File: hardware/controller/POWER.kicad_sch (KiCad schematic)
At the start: 21 parts, among them IC201 TPS63000IDRCRQ1, J201 1769

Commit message: a
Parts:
- added NT201: NetTie, NetTie:NetTie-2_SMD_Pad0.5mm, symbol SamacSys_Parts:NetTie
- D201: footprint SMF50A_R1_00001 -> SamacSys_Parts:SMF50A_R1_00001
- IC201: footprint SamacSys_Parts:TPS63000IDRCRQ1 -> TPS63000IDRCRQ1
- R201: footprint RESC1608X55N -> SamacSys_Parts:RESC1608X55N
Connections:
- net GND: now also NT201.1
- net GNDPWR: now also NT201.2
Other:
- note removed: "Connect control ground to common ground near GND pin"
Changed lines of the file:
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@@
 		)
 	)
-	(text "Connect control ground to \ncommon ground near GND pin"
-		(exclude_from_sim no)
-		(at 247.396 148.336 0)
-		(effects
-			(font
-				(size 1.27 1.27)
-			)
-		)
-	)
 	(text "Hierarchical Pins"
 		(exclude_from_sim no)
@@
 	)
 	(junction
+		(at 219.71 146.05)
+		(diameter 0)
+		(color 0 0 0 0)
+	)
+	(junction
 		(at 133.35 110.49)
 		(diameter 0)
@@
 	)
 	(junction
+		(at 209.55 146.05)
+		(diameter 0)
+		(color 0 0 0 0)
+	)
+	(junction
+		(at 204.47 146.05)
+		(diameter 0)
+		(color 0 0 0 0)
+	)
+	(junction
 		(at 246.38 114.3)
 		(diameter 0)
@@
 	)
 	(junction
-		(at 209.55 146.05)
-		(diameter 0)
-		(color 0 0 0 0)
-	)
-	(junction
 		(at 250.19 124.46)
 		(diameter 0)
@@
 	(wire
 		(pts
-			(xy 207.01 146.05) (xy 207.01 142.24)
-		)
-		(stroke
-			(width 0)
-			(type default)
-		)
-	)
-	(wire
-		(pts
 			(xy 186.69 110.49) (xy 195.58 110.49)
 		)
@@
 	(wire
 		(pts
-			(xy 204.47 142.24) (xy 204.47 149.86)
+			(xy 204.47 142.24) (xy 204.47 146.05)
 		)
 		(stroke
@@
 	(wire
 		(pts
-			(xy 207.01 146.05) (xy 209.55 146.05)
+			(xy 88.9 110.49) (xy 91.44 110.49)
 		)
 		(stroke
@@
 	(wire
 		(pts
-			(xy 88.9 110.49) (xy 91.44 110.49)
+			(xy 186.69 119.38) (xy 186.69 121.92)
 		)
 		(stroke
@@
 	(wire
 		(pts
-			(xy 186.69 119.38) (xy 186.69 121.92)
+			(xy 208.28 146.05) (xy 209.55 146.05)
 		)
 		(stroke
@@
 	(wire
 		(pts
+			(xy 222.25 146.05) (xy 219.71 146.05)
+		)
+		(stroke
+			(width 0)
+			(type default)
+		)
+	)
+	(wire
+		(pts
 			(xy 133.35 110.49) (xy 139.7 110.49)
 		)
@@
 	(wire
 		(pts
+			(xy 222.25 142.24) (xy 222.25 146.05)
+		)
+		(stroke
+			(width 0)
+			(type default)
+		)
+	)
+	(wire
+		(pts
 			(xy 173.99 114.3) (xy 173.99 110.49)
 		)
@@
 	(wire
 		(pts
+			(xy 204.47 146.05) (xy 204.47 149.86)
+		)
+		(stroke
+			(width 0)
+			(type default)
+		)
+	)
+	(wire
+		(pts
 			(xy 33.02 71.12) (xy 76.2 71.12)
 		)
@@
 	)
 	(symbol
-		(lib_id "power:GNDPWR")
-		(at 252.73 151.13 0)
-		(unit 1)
-		(exclude_from_sim no)
-		(in_bom yes)
-		(on_board yes)
-		(dnp no)
-		(fields_autoplaced yes)
-		(property "Reference" "#PWR0217"
-			(at 252.73 156.21 0)
-			(effects
-				(font
-					(size 1.27 1.27)
-				)
-				(hide yes)
-			)
-		)
-		(property "Value" "GNDPWR"
-			(at 252.603 154.94 0)
-			(effects
-				(font
-					(size 1.27 1.27)
-				)
-			)
-		)
-		(property "Footprint" ""
-			(at 252.73 152.4 0)
-			(effects
-				(font
-					(size 1.27 1.27)
-				)
-				(hide yes)
-			)
-		)
-		(property "Datasheet" ""
-			(at 252.73 152.4 0)
-			(effects
-				(font
-					(size 1.27 1.27)
-				)
-				(hide yes)
-			)
-		)
-		(property "Description" "Power symbol creates a global label with name \"GNDPWR\" , global ground"
-			(at 252.73 151.13 0)
-			(effects
-				(font
-					(size 1.27 1.27)
-				)
-				(hide yes)
-			)
-		)
-		(pin "1"
-		)
-		(instances
-			(project "controller"
-				(path "/869bea87-c885-4ead-826b-3f34ceacafad/e70789ad-230b-4d46-b635-87f45083e468"
-					(reference "#PWR0217")
-					(unit 1)
-				)
-			)
-		)
-	)
-	(symbol
 		(lib_id "Device:R")
 		(at 186.69 114.3 0)
@@
 			)
 		)
-		(property "Footprint" "RESC1608X55N"
+		(property "Footprint" "SamacSys_Parts:RESC1608X55N"
 			(at 200.66 210.49 0)
 			(effects
@@
 			)
 		)
-		(property "Footprint" "SMF50A_R1_00001"
+		(property "Footprint" "SamacSys_Parts:SMF50A_R1_00001"
 			(at -42.85 124.46 0)
 			(effects
@@
 	(symbol
 		(lib_id "power:GND")
-		(at 241.3 151.13 0)
-		(unit 1)
-		(exclude_from_sim no)
-		(in_bom yes)
-		(on_board yes)
-		(dnp no)
-		(fields_autoplaced yes)
-		(property "Reference" "#PWR0215"
-			(at 241.3 157.48 0)
-			(effects
-				(font
-					(size 1.27 1.27)
-				)
-				(hide yes)
-			)
-		)
-		(property "Value" "GND"
-			(at 241.3 156.21 0)
-			(effects
-				(font
-					(size 1.27 1.27)
-				)
-			)
-		)
-		(property "Footprint" ""
-			(at 241.3 151.13 0)
-			(effects
-				(font
-					(size 1.27 1.27)
-				)
-				(hide yes)
-			)
-		)
-		(property "Datasheet" ""
-			(at 241.3 151.13 0)
-			(effects
-				(font
-					(size 1.27 1.27)
-				)
-				(hide yes)
-			)
-		)
-		(property "Description" "Power symbol creates a global label with name \"GND\" , ground"
-			(at 241.3 151.13 0)
-			(effects
-				(font
-					(size 1.27 1.27)
-				)
-				(hide yes)
-			)
-		)
-		(pin "1"
-		)
-		(instances
-			(project "controller"
-				(path "/869bea87-c885-4ead-826b-3f34ceacafad/e70789ad-230b-4d46-b635-87f45083e468"
-					(reference "#PWR0215")
-					(unit 1)
-				)
-			)
-		)
-	)
-	(symbol
-		(lib_id "power:GND")
 		(at 139.7 134.62 0)
 		(unit 1)
@@
 	)
 	(symbol
+		(lib_id "SamacSys_Parts:NetTie")
+		(at 207.01 146.05 0)
+		(unit 1)
+		(exclude_from_sim no)
+		(in_bom no)
+		(on_board yes)
+		(dnp no)
+		(property "Reference" "NT201"
+			(at 197.358 142.24 0)
+			(effects
+				(font
+					(size 1.27 1.27)
+				)
+			)
+		)
+		(property "Value" "NetTie"
+			(at 197.358 144.78 0)
+			(effects
+				(font
+					(size 1.27 1.27)
+				)
+			)
+		)
+		(property "Footprint" "NetTie:NetTie-2_SMD_Pad0.5mm"
+			(at 207.01 146.05 0)
+			(effects
+				(font
+					(size 1.27 1.27)
+				)
+				(hide yes)
+			)
+		)
+		(property "Datasheet" "~"
+			(at 207.01 146.05 0)
+			(effects
+				(font
+					(size 1.27 1.27)
+				)
+				(hide yes)
+			)
+		)
+		(property "Description" "Net tie, 2 pins"
+			(at 207.01 146.05 0)
+			(effects
+				(font
+					(size 1.27 1.27)
+				)
+				(hide yes)
+			)
+		)
+		(pin "1"
+		)
+		(pin "2"
+		)
+		(instances
+			(project ""
+				(path "/869bea87-c885-4ead-826b-3f34ceacafad/e70789ad-230b-4d46-b635-87f45083e468"
+					(reference "NT201")
+					(unit 1)
+				)
+			)
+		)
+	)
+	(symbol
 		(lib_id "Device:L")
 		(at 213.36 95.25 90)
@@
 			)
 		)
-		(property "Footprint" "SamacSys_Parts:TPS63000IDRCRQ1"
+		(property "Footprint" "TPS63000IDRCRQ1"
 			(at 227.33 199.06 0)
 			(effects

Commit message: kicad why crash
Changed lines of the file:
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@@
+	)
+	(junction
+		(at 250.19 133.35)
+		(diameter 0)
+		(color 0 0 0 0)
 	)
 	(junction
@@
 	(wire
 		(pts
-			(xy 250.19 134.62) (xy 250.19 124.46)
+			(xy 250.19 134.62) (xy 250.19 133.35)
 		)
 		(stroke
@@
 	(wire
 		(pts
+			(xy 250.19 133.35) (xy 250.19 124.46)
+		)
+		(stroke
+			(width 0)
+			(type default)
+		)
+	)
+	(wire
+		(pts
 			(xy 179.07 72.39) (xy 181.61 72.39)
 		)
@@
 		(pts
 			(xy 195.58 121.92) (xy 195.58 124.46)
+		)
+		(stroke
+			(width 0)
+			(type default)
+		)
+	)
+	(wire
+		(pts
+			(xy 250.19 133.35) (xy 256.54 133.35)
 		)
 		(stroke
@@
 					(unit 1)
 				)
+			)
+		)
+	)
+	(symbol
+		(lib_id "power:PWR_FLAG")
+		(at 256.54 133.35 0)
+		(unit 1)
+		(exclude_from_sim no)
+		(in_bom yes)
+		(on_board yes)
+		(dnp no)
+		(fields_autoplaced yes)
+		(property "Reference" "#FLG0203"
+			(at 256.54 131.445 0)
+			(effects
+				(font
+					(size 1.27 1.27)
+				)
+				(hide yes)
+			)
+		)
+		(property "Value" "PWR_FLAG"
+			(at 256.54 128.27 0)
+			(effects
+				(font
+					(size 1.27 1.27)
+				)
+			)
+		)
+		(property "Footprint" ""
+			(at 256.54 133.35 0)
+			(effects
+				(font
+					(size 1.27 1.27)
+				)
+				(hide yes)
+			)
+		)
+		(property "Datasheet" "~"
+			(at 256.54 133.35 0)
+			(effects
+				(font
+					(size 1.27 1.27)
+				)
+				(hide yes)
+			)
+		)
+		(property "Description" "Special symbol for telling ERC where power comes from"
+			(at 256.54 133.35 0)
+			(effects
+				(font
+					(size 1.27 1.27)
+				)
+				(hide yes)
+			)
+		)
+		(pin "1"
+		)
+		(instances
+			(project ""
+				(path "/869bea87-c885-4ead-826b-3f34ceacafad/e70789ad-230b-4d46-b635-87f45083e468"
+					(reference "#FLG0203")
+					(unit 1)
+				)

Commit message: save before nuke
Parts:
- IC101: renamed from IC201; footprint TPS63000IDRCRQ1 -> SamacSys_Parts:TPS63000IDRCRQ1
- renumbered C201 to C101, C202 to C102, C203 to C103, C204 to C104, C205 to C105, C206 to C106, C207 to C107, D201 to D101, D202 to D102, D203 to D103, J201 to J101, L201 to L101, NT201 to NT101, R201 to R101, R202 to R102, R203 to R103, TP201 to TP101, TP202 to TP102, TP203 to TP103, TP204 to TP104, TP205 to TP105

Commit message: done but need to add stitching vias
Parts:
- TP101, TP102, TP103, TP104, TP105: footprint TestPoint:TestPoint_Pad_1.0x1.0mm -> SamacSys_Parts:TestPoint_Pad_1.0x1.0mm
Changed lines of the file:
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@@
 			)
 		)
-		(property "Footprint" "TestPoint:TestPoint_Pad_1.0x1.0mm"
+		(property "Footprint" "SamacSys_Parts:TestPoint_Pad_1.0x1.0mm"
 			(at 190.5 62.23 0)
 			(effects
@@
 			)
 		)
-		(property "Footprint" "TestPoint:TestPoint_Pad_1.0x1.0mm"
+		(property "Footprint" "SamacSys_Parts:TestPoint_Pad_1.0x1.0mm"
 			(at 81.28 110.49 0)
 			(effects
@@
 			)
 		)
-		(property "Footprint" "TestPoint:TestPoint_Pad_1.0x1.0mm"
+		(property "Footprint" "SamacSys_Parts:TestPoint_Pad_1.0x1.0mm"
 			(at 81.28 71.12 0)
 			(effects
@@
 			)
 		)
-		(property "Footprint" "TestPoint:TestPoint_Pad_1.0x1.0mm"
+		(property "Footprint" "SamacSys_Parts:TestPoint_Pad_1.0x1.0mm"
 			(at 138.43 110.49 0)
 			(effects
@@
 			)
 		)
-		(property "Footprint" "TestPoint:TestPoint_Pad_1.0x1.0mm"
+		(property "Footprint" "SamacSys_Parts:TestPoint_Pad_1.0x1.0mm"
 			(at 190.5 72.39 0)
 			(effects

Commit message: forgor
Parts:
- NT101: footprint NetTie:NetTie-2_SMD_Pad0.5mm -> SamacSys_Parts:NetTie-2_Pad0.3mm
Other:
- note added: "3v3 Generation"
- note added: "Power Inputs"
- moved on the sheet: C101, C102, C103, C104, C105, C106, C107, D101, D102, D103, IC101, J101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

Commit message: clean up DRC. need to add stitching vias and figure out why inner ground plane isnt connected to F.Cu pour
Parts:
- renumbered C101 to C201, C102 to C202, C103 to C203, C104 to C204, C105 to C205, C106 to C206, C107 to C207, D101 to D201, D102 to D202, D103 to D203, IC101 to IC201, J101 to J201, L101 to L201, NT101 to NT201, R101 to R201, R102 to R202, R103 to R203, TP102 to TP201, TP104 to TP202, TP105 to TP203, TP101 to TP204, TP103 to TP205

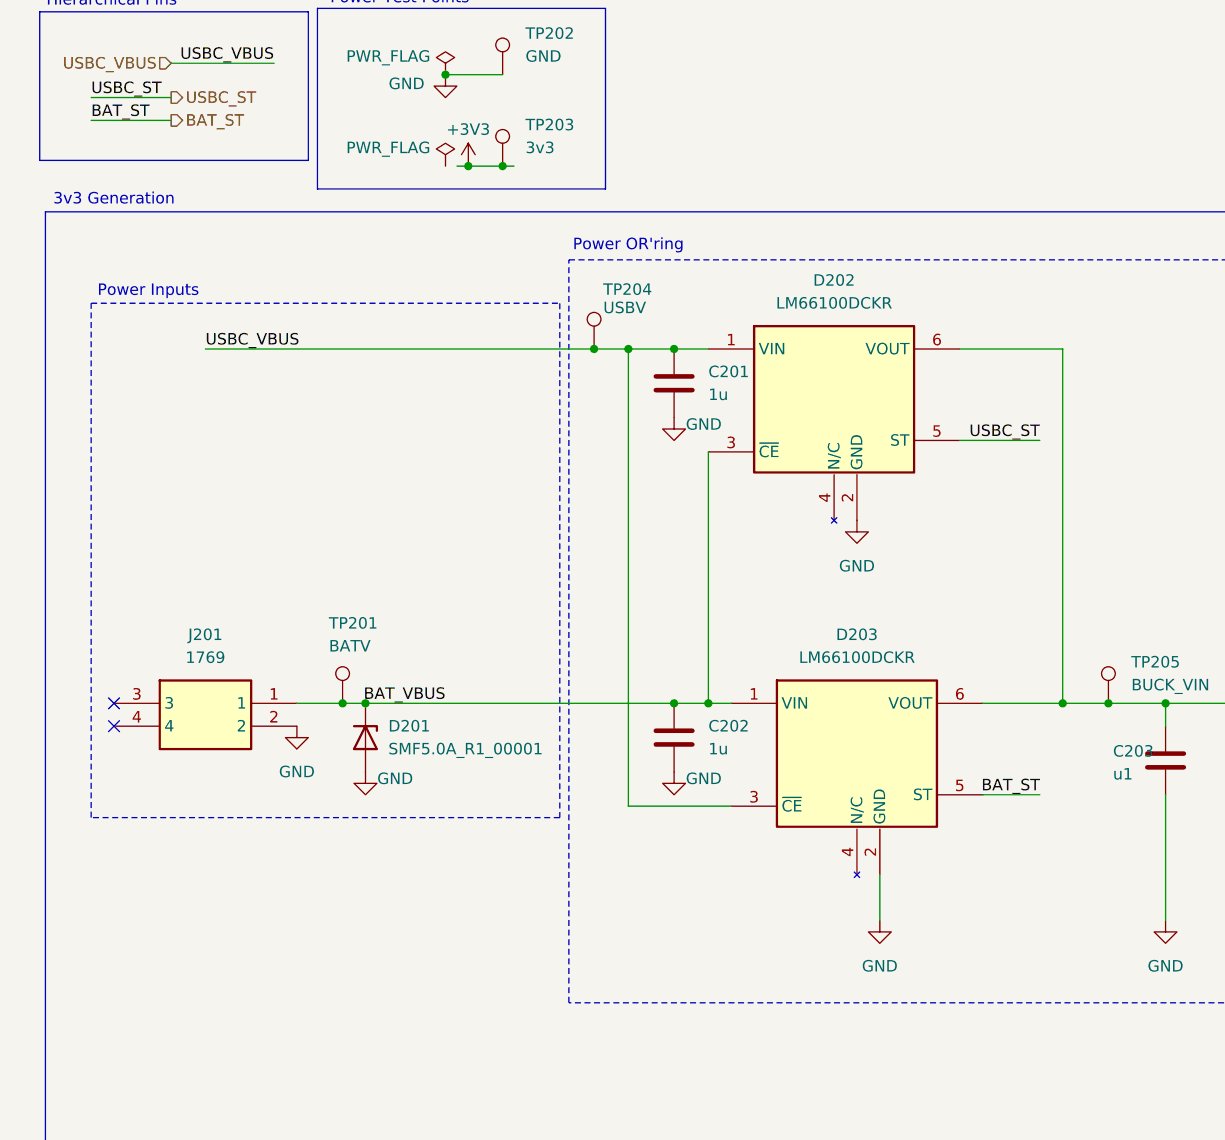
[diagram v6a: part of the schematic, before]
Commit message: save before axing motor driver ic's
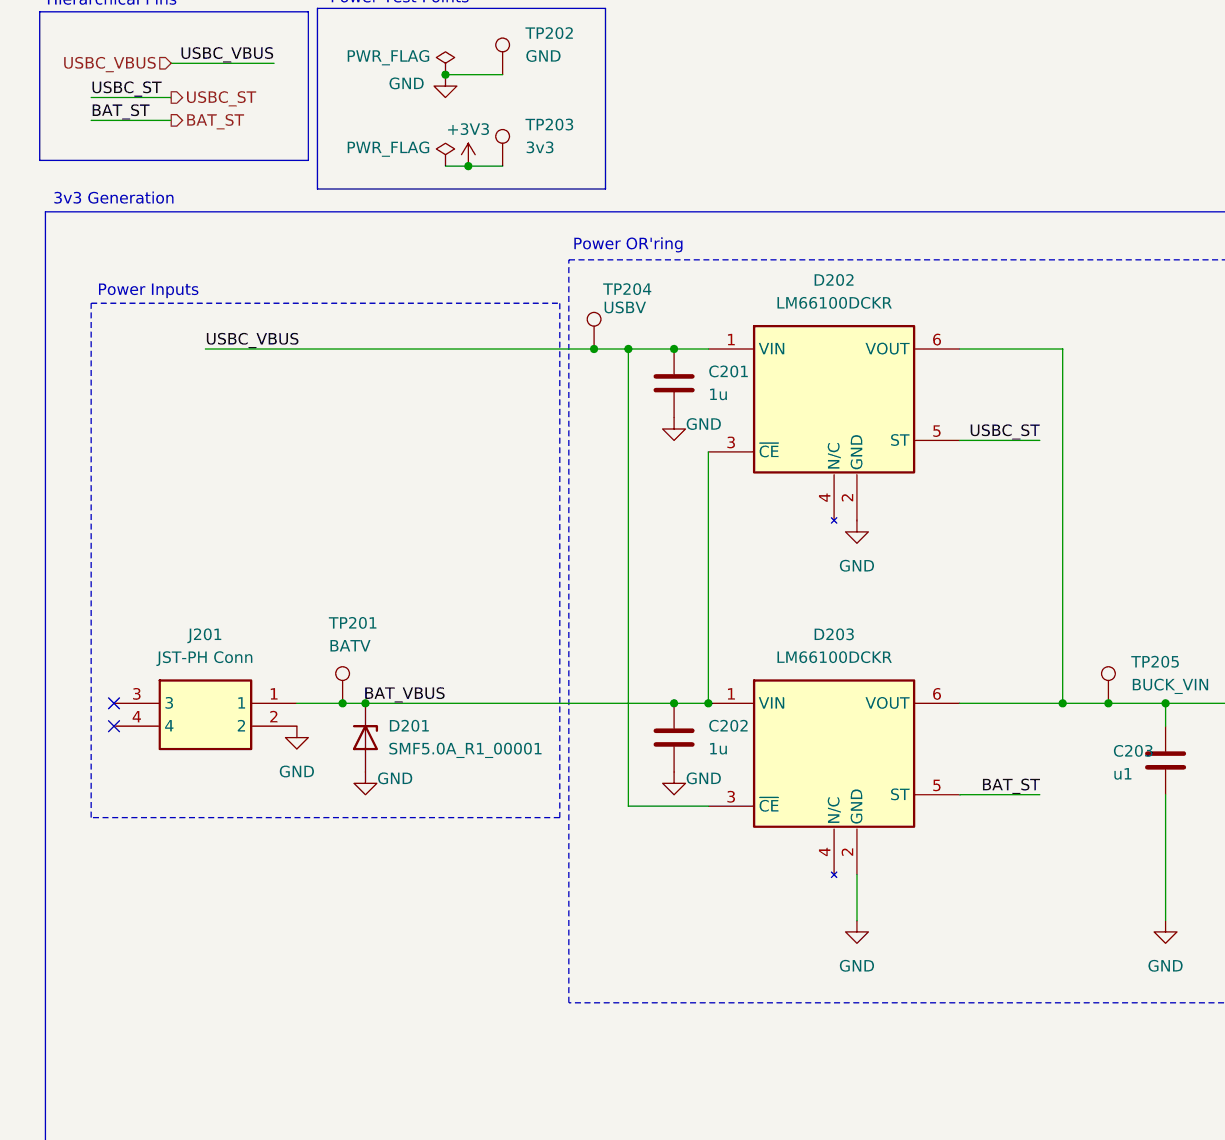
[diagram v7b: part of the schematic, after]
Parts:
- J201: value 1769 -> JST-PH Conn
- R202: Mouser Price/Stock https://www.mouser.com/ProductDetail/ROHM-Semiconductor/SFR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 -> https://www.mouser.co.uk/ProductDetail/ROHM-Semiconductor/S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
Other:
- moved on the sheet: D203
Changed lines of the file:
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@@
 	)
 	(junction
-		(at 66.04 34.29)
-		(diameter 0)
-		(color 0 0 0 0)
-	)
-	(junction
 		(at 212.09 129.54)
 		(diameter 0)
@@
 	(wire
 		(pts
-			(xy 80.01 105.41) (xy 91.44 105.41)
+			(xy 80.01 105.41) (xy 88.9 105.41)
 		)
 		(stroke
@@
 	(wire
 		(pts
-			(xy 119.38 93.98) (xy 128.27 93.98)
+			(xy 116.84 93.98) (xy 128.27 93.98)
 		)
 		(stroke
@@
 	(wire
 		(pts
-			(xy 88.9 93.98) (xy 91.44 93.98)
-		)
-		(stroke
-			(width 0)
-			(type default)
-		)
-	)
-	(wire
-		(pts
 			(xy 186.69 102.87) (xy 186.69 105.41)
 		)
@@
 	(wire
 		(pts
-			(xy 60.96 34.29) (xy 62.23 34.29)
-		)
-		(stroke
-			(width 0)
-			(type default)
-		)
-	)
-	(wire
-		(pts
 			(xy 231.14 91.44) (xy 231.14 78.74)
 		)
@@
 	(wire
 		(pts
-			(xy 119.38 104.14) (xy 125.73 104.14)
+			(xy 116.84 104.14) (xy 125.73 104.14)
 		)
 		(stroke
@@
 	(wire
 		(pts
-			(xy 66.04 34.29) (xy 67.31 34.29)
-		)
-		(stroke
-			(width 0)
-			(type default)
-		)
-	)
-	(wire
-		(pts
 			(xy 246.38 97.79) (xy 254 97.79)
 		)
@@
 	(wire
 		(pts
-			(xy 107.95 118.11) (xy 107.95 113.03)
+			(xy 105.41 118.11) (xy 105.41 113.03)
 		)
 		(stroke
@@
 	(wire
 		(pts
+			(xy 59.69 34.29) (xy 62.23 34.29)
+		)
+		(stroke
+			(width 0)
+			(type default)
+		)
+	)
+	(wire
+		(pts
 			(xy 204.47 129.54) (xy 204.47 133.35)
 		)
@@
 			)
 		)
-		(property "Datasheet" "https://www.rohm.com/datasheet?p=SFR03EZPJ&dist=Mouser&media=referral&source=mouser.com&campaign=Mouser"
+		(property "Datasheet" "https://www.rohm.com/datasheet?p=SFR03EZPJ&dist=Mouser&media=referral&source=mouser.co.uk&campaign=Mouser"
 			(at 236.22 104.14 0)
 			(effects
@@
 			)
 		)
-		(property "Mouser Price/Stock" "https://www.mouser.com/ProductDetail/ROHM-Semiconductor/SFR03EZPJ105?qs=sGAEpiMZZMvdGkrng054t7z4BkURc4Lzl1WyxFadKNwUJSL%2FdgazDw%3D%3D"
+		(property "Mouser Price/Stock" "https://www.mouser.co.uk/ProductDetail/ROHM-Semiconductor/SFR03EZPJ105?qs=sGAEpiMZZMvdGkrng054t7z4BkURc4Lzl1WyxFadKNwUJSL%2FdgazDw%3D%3D"
 			(at 236.22 104.14 0)
 			(effects
@@
 	(symbol
 		(lib_id "power:GND")
-		(at 107.95 118.11 0)
+		(at 105.41 118.11 0)
 		(unit 1)
 		(exclude_from_sim no)
@@
 		(fields_autoplaced yes)
 		(property "Reference" "#PWR0208"
-			(at 107.95 124.46 0)
+			(at 105.41 124.46 0)
 			(effects
 				(font
@@
 		)
 		(property "Value" "GND"
-			(at 107.95 123.19 0)
+			(at 105.41 123.19 0)
 			(effects
 				(font
@@
 		)
 		(property "Footprint" ""
-			(at 107.95 118.11 0)
+			(at 105.41 118.11 0)
 			(effects
 				(font
@@
 		)
 		(property "Datasheet" ""
-			(at 107.95 118.11 0)
+			(at 105.41 118.11 0)
 			(effects
 				(font
@@
 		)
 		(property "Description" "Power symbol creates a global label with name \"GND\" , ground"
-			(at 107.95 118.11 0)
+			(at 105.41 118.11 0)
 			(effects
 				(font
@@
 			)
 		)
-		(property "Value" "1769"
+		(property "Value" "JST-PH Conn"
 			(at 33.02 88.9 0)
 			(effects
@@
 	(symbol
 		(lib_id "SamacSys_Parts:LM66100DCKR")
-		(at 91.44 93.98 0)
+		(at 88.9 93.98 0)
 		(unit 1)
 		(exclude_from_sim no)
@@
 		(fields_autoplaced yes)
 		(property "Reference" "D203"
-			(at 105.41 86.36 0)
+			(at 102.87 86.36 0)
 			(effects
 				(font
@@
 		)
 		(property "Value" "LM66100DCKR"
-			(at 105.41 88.9 0)
+			(at 102.87 88.9 0)
 			(effects
 				(font
@@
 		)
 		(property "Footprint" "SamacSys_Parts:SOP65P210X110-6N"
-			(at 115.57 188.9 0)
+			(at 113.03 188.9 0)
 			(effects
 				(font
@@
 		)
 		(property "Datasheet" "http://www.ti.com/lit/gpn/LM66100"
-			(at 115.57 288.9 0)
+			(at 113.03 288.9 0)
 			(effects
 				(font
@@
 		)
 		(property "Description" "+/-6-V, Low IQ ideal diode with input polarity protection"
-			(at 91.44 93.98 0)
+			(at 88.9 93.98 0)
 			(effects
 				(font
@@
 		)
 		(property "Height" "1.1"
-			(at 115.57 488.9 0)
+			(at 113.03 488.9 0)
 			(effects
 				(font
@@
 		)
 		(property "Mouser Part Number" "595-LM66100DCKR"
-			(at 115.57 588.9 0)
+			(at 113.03 588.9 0)
 			(effects
 				(font
@@
 		)
 		(property "Mouser Price/Stock" "https://www.mouser.co.uk/ProductDetail/Texas-Instruments/LM66100DCKR?qs=vLWxofP3U2y2yPPrXoBBoA%3D%3D"
-			(at 115.57 688.9 0)
+			(at 113.03 688.9 0)
 			(effects
 				(font
@@
 		)
 		(property "Manufacturer_Name" "Texas Instruments"
-			(at 115.57 788.9 0)
+			(at 113.03 788.9 0)
 			(effects
 				(font
@@
 		)
 		(property "Manufacturer_Part_Number" "LM66100DCKR"
-			(at 115.57 888.9 0)
+			(at 113.03 888.9 0)
 			(effects
 				(font
